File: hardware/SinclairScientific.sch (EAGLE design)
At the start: 93 parts, among them J1 JSTPH, J3 USB-MICRO, U2 SPX3819-3.3, U3 MCP73831T-2ACI/OT, U4 ATSAMD21G18, U5 W25Q128JVSO, X2 32.768

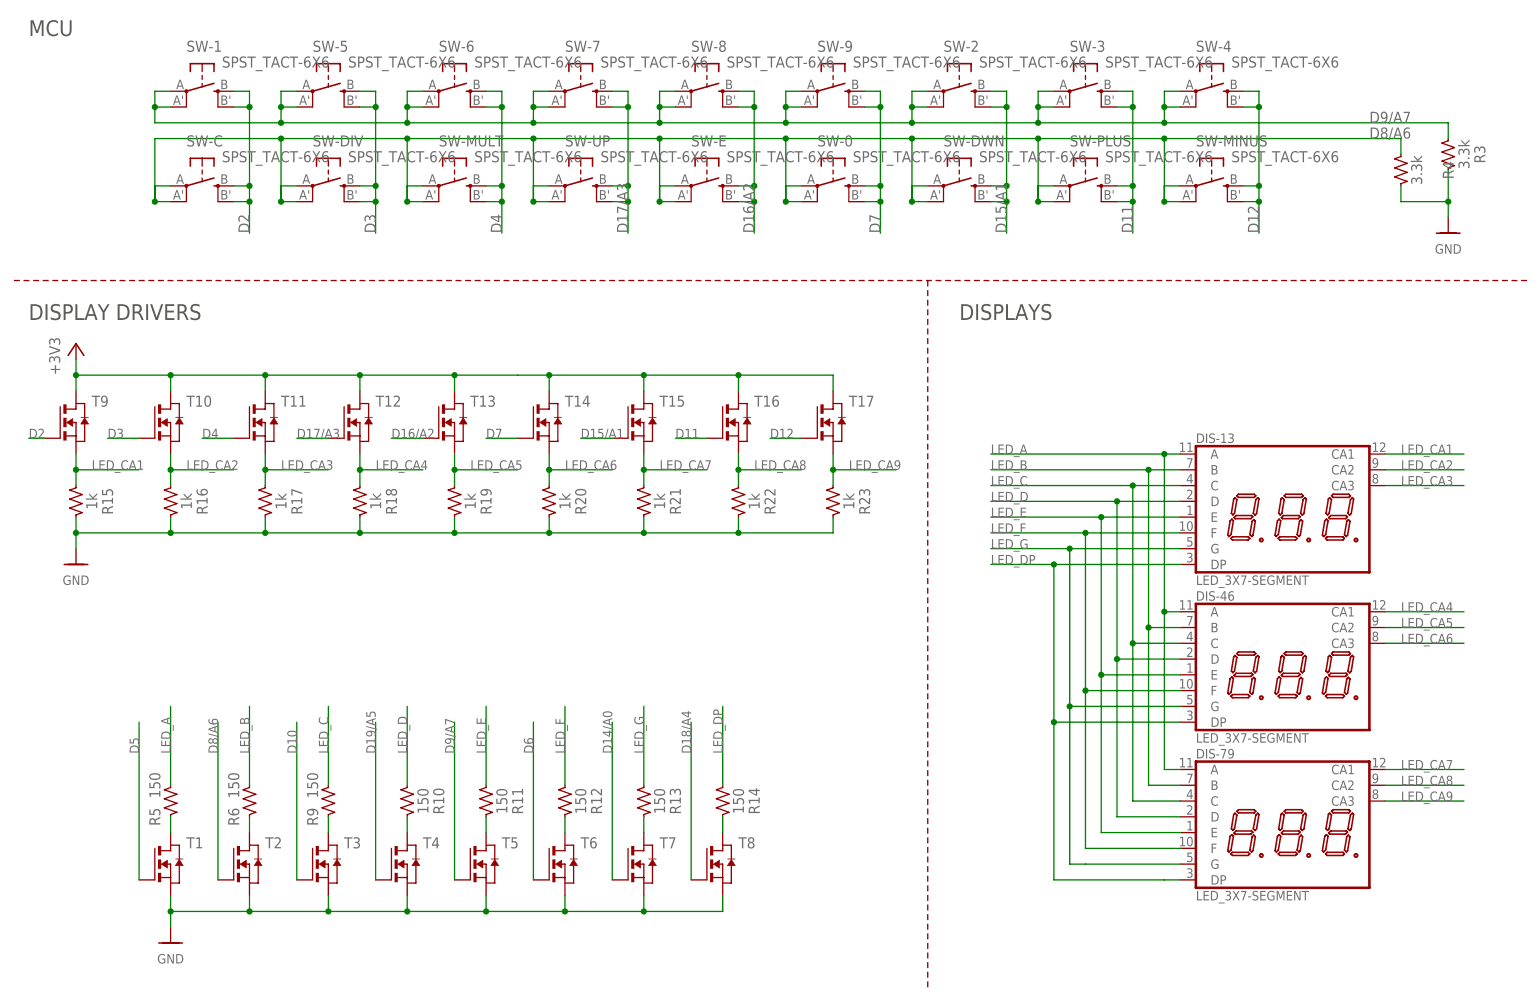
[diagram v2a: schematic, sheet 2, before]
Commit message: Moved displays to their own sch/brd files, nearly finished routing main board
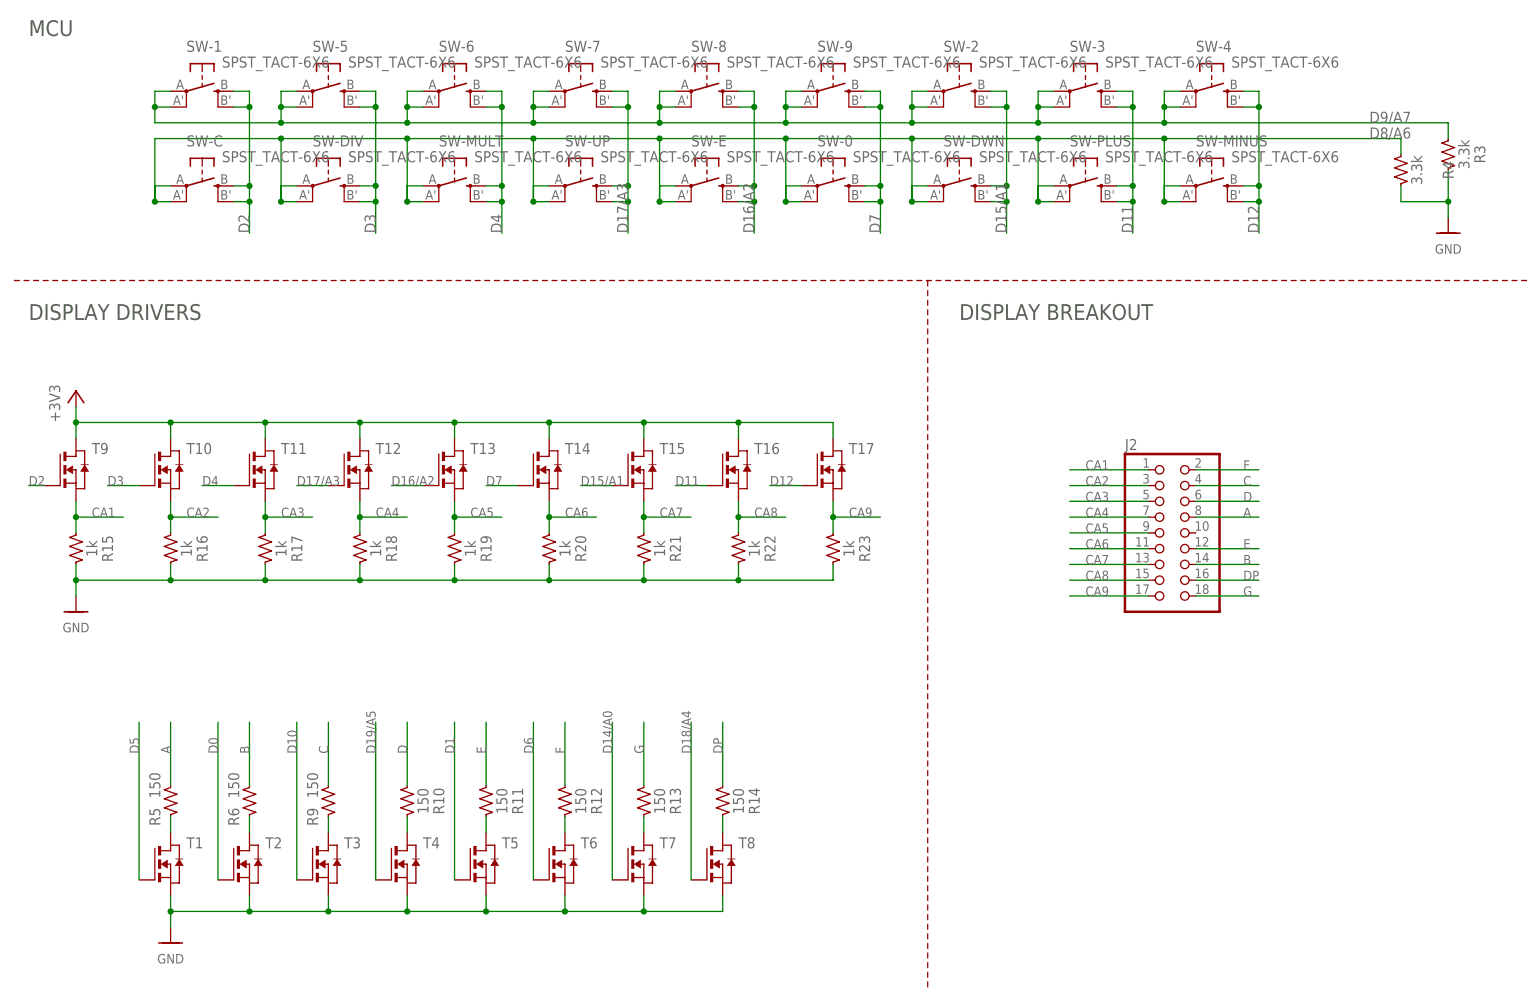
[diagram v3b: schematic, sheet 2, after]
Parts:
- removed DIS-13, DIS-46, DIS-79: LED_3X7-SEGMENT, SinclairScientific:LED_3X7-SEGMENT
- removed U$34: FIDUCIAL"", SinclairScientific:FIDUCIAL""
- added J2: (no value), SinclairScientific:PINHD-2X9-2MM-SMD
- added S1: SPST_SLIDE, SinclairScientific:SPST_SLIDE
- D1: MFG (none) -> ON Semiconductor; MPN (none) -> MBR120VLSFT1G; PN-DK (none) -> MBR120VLSFT1GOSCT-ND
- R2: value 2.2k -> 1k
- R8: value 10K\ -> 3.3k
- U2: MFG (none) -> MaxLinear, Inc.; MPN (none) -> SPX3819M5-L-3-3/TR; PN-DK (none) -> 1016-1873-1-ND
- U3: MFG (none) -> Microchip Technology; MPN (none) -> MCP73831T-2ACI/OT; PN-DK (none) -> MCP73831T-2ACI/OTCT-ND
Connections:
- net D39 renamed D39/!MEM_CS
- net N$5 renamed EXTAL32
- net N$7 renamed XTAL32
- net USB_DM renamed USBD_N
- net USB_DP renamed USBD_P
- removed net LED_A: DIS-13.A, DIS-46.A, DIS-79.A, R5.1
- removed net LED_B: DIS-13.B, DIS-46.B, DIS-79.B, R6.1
- removed net LED_C: DIS-13.C, DIS-46.C, DIS-79.C, R9.1
- removed net LED_CA1: DIS-13.CA1, R15.1, T9.S
- removed net LED_CA2: DIS-13.CA2, R16.1, T10.S
- removed net LED_CA3: DIS-13.CA3, R17.1, T11.S
- removed net LED_CA4: DIS-46.CA1, R18.1, T12.S
- removed net LED_CA5: DIS-46.CA2, R19.1, T13.S
- removed net LED_CA6: DIS-46.CA3, R20.1, T14.S
- removed net LED_CA7: DIS-79.CA1, R21.1, T15.S
- removed net LED_CA8: DIS-79.CA2, R22.1, T16.S
- removed net LED_CA9: DIS-79.CA3, R23.1, T17.S
- removed net LED_D: DIS-13.D, DIS-46.D, DIS-79.D, R10.1
- removed net LED_DP: DIS-13.DP, DIS-46.DP, DIS-79.DP, R14.1
- removed net LED_E: DIS-13.E, DIS-46.E, DIS-79.E, R11.1
- removed net LED_F: DIS-13.F, DIS-46.F, DIS-79.F, R12.1
- removed net LED_G: DIS-13.G, DIS-46.G, DIS-79.G, R13.1
- new net A: J2.8, R5.1
- new net B: J2.14, R6.1
- new net C: J2.4, R9.1
- new net CA1: J2.1, R15.1, T9.S
- new net CA2: J2.3, R16.1, T10.S
- new net CA3: J2.5, R17.1, T11.S
- new net CA4: J2.7, R18.1, T12.S
- new net CA5: J2.9, R19.1, T13.S
- new net CA6: J2.11, R20.1, T14.S
- new net CA7: J2.13, R21.1, T15.S
- new net CA8: J2.15, R22.1, T16.S
- new net CA9: J2.17, R23.1, T17.S
- new net D: J2.6, R10.1
- new net DP: J2.16, R14.1
- new net E: J2.12, R11.1
- new net F: J2.2, R12.1
- new net G: J2.18, R13.1
- new net VBUS_SW: C6.1, S1.1, U2.EN, U2.IN
- net D0: now also T2.G
- net D1: now also T5.G
- net D8/A6: no longer T2.G
- net D9/A7: no longer T5.G
- net VBUS: now also S1.2; no longer C6.1, U2.EN, U2.IN
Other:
- note added: "DISPLAY BREAKOUT"
- note removed: "DISPLAYS"
- moved on the sheet: C6, C7, C8, D1, L1, R1, R15, R16, R17, R18, R19, R20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

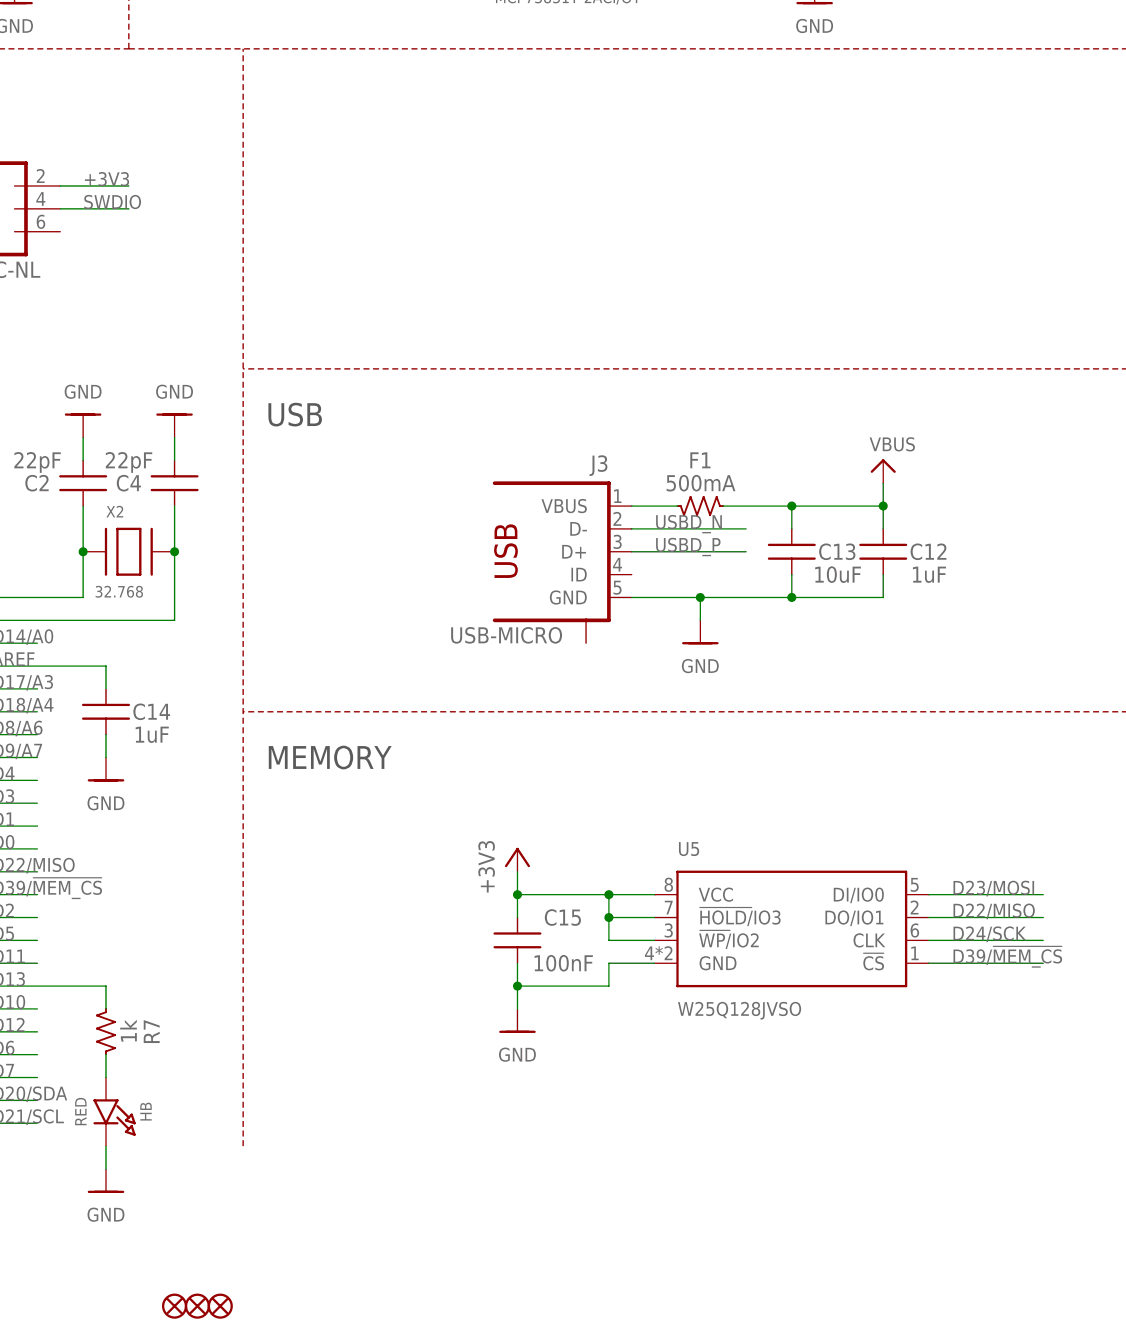
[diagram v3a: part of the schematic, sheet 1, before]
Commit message: Added some silkscreen labels and logo
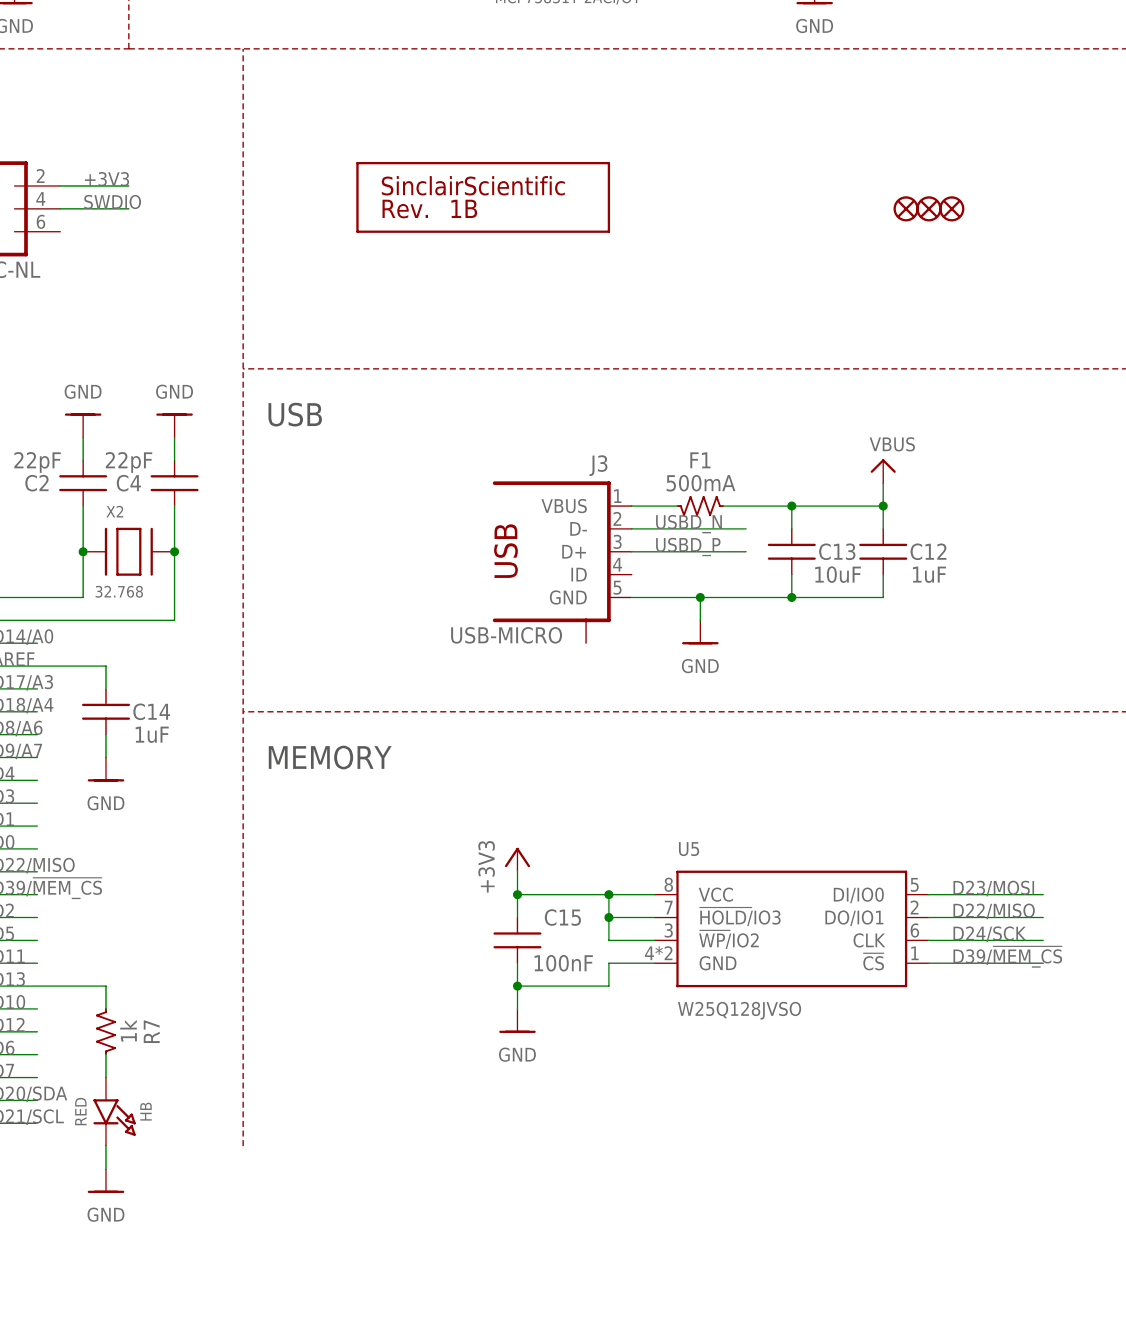
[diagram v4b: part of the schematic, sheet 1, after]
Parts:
- added U$18: SILK_QC, SinclairScientific:SILK_QC
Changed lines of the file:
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@@
 <layer number="112" name="tSilk" color="7" fill="1" visible="yes" active="yes"/>
 <layer number="113" name="ReferenceLS" color="7" fill="1" visible="no" active="no"/>
+<layer number="114" name="Badge_Outline" color="7" fill="1" visible="no" active="yes"/>
+<layer number="115" name="ReferenceISLANDS" color="7" fill="1" visible="no" active="yes"/>
 <layer number="116" name="Patch_BOT" color="9" fill="4" visible="yes" active="yes"/>
 <layer number="118" name="Rect_Pads" color="7" fill="1" visible="no" active="no"/>
@@
 </part>
 <part name="S1" library="SinclairScientific" deviceset="SPST_SLIDE" device=""/>
+<part name="U$18" library="SinclairScientific" deviceset="SILK_QC" device="">
+<attribute name="PRODUCT" value="SinclairScientific"/>
+<attribute name="REV" value="1B"/>
+</part>
 </parts>
 <sheets>
@@
 <attribute name="VALUE" x="119.38" y="17.78" size="1.524" layer="96" rot="MR0" align="center"/>
 </instance>
-<instance part="U$35" gate="G$1" x="132.08" y="7.62"/>
+<instance part="U$35" gate="G$1" x="213.36" y="129.54"/>
 <instance part="+3V4" gate="G$1" x="91.44" y="172.72" rot="MR0">
 <attribute name="VALUE" x="93.98" y="167.64" size="1.778" layer="96" rot="MR90"/>
@@
 <attribute name="VALUE" x="20.32" y="104.14" size="1.524" layer="96" align="center"/>
 </instance>
-<instance part="U$7" gate="G$1" x="127" y="7.62"/>
+<instance part="U$7" gate="G$1" x="208.28" y="129.54"/>
 <instance part="C9" gate="G$1" x="30.48" y="116.84">
 <attribute name="NAME" x="35.56" y="116.84" size="1.778" layer="95" align="center"/>
@@
 <attribute name="SECTION" x="199.39" y="11.43" size="2.54" layer="94" align="center-left"/>
 </instance>
-<instance part="U$2" gate="G$1" x="129.54" y="7.62"/>
+<instance part="U$2" gate="G$1" x="210.82" y="129.54"/>
 <instance part="U5" gate="G$1" x="195.58" y="50.8">
 <attribute name="NAME" x="182.88" y="58.42" size="1.524" layer="95" align="center-left"/>
@@
 <attribute name="VALUE" x="27.94053125" y="160.01893125" size="1.27026875" layer="96"/>
 </instance>
+<instance part="U$18" gate="G$1" x="147.32" y="132.08">
+<attribute name="PRODUCT" x="149.86" y="132.08" size="2.032" layer="94" align="center-left"/>
+<attribute name="REV" x="157.48" y="129.54" size="2.032" layer="94" align="center-left"/>
+</instance>
 </instances>
